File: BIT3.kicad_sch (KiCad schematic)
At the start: 46 parts, among them J1 Conn_02x04_Odd_Even, J2 Conn_01x02_Pin, Q1 2SC1815, SW1 SW_SPDT, SW2 SW_Push, SW3 SW_Push, U2 SG-107F, U3 SG-107F, U4 SG-107F, U5 SG-107F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

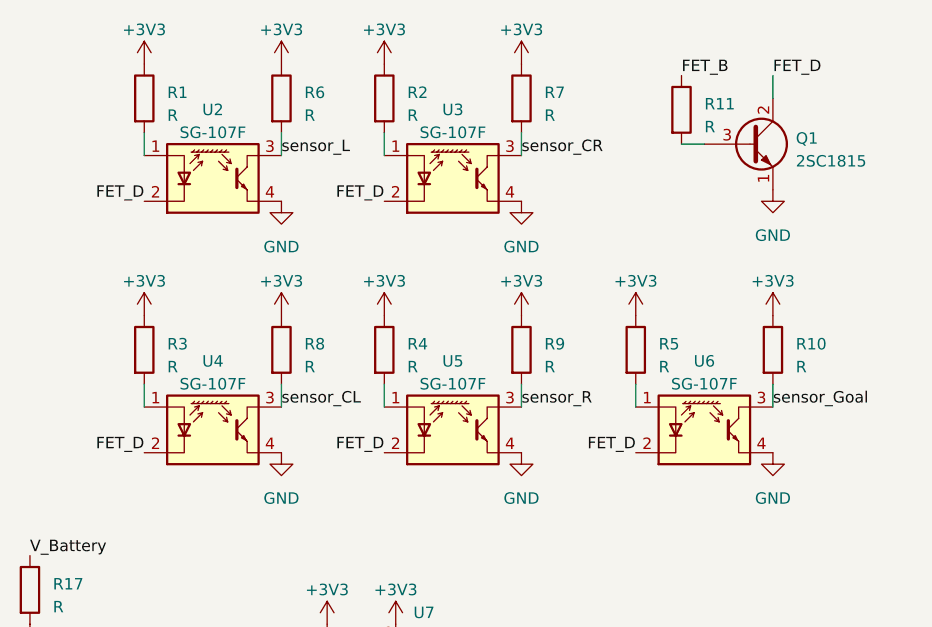
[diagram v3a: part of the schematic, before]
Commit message: フォトセンサを変更
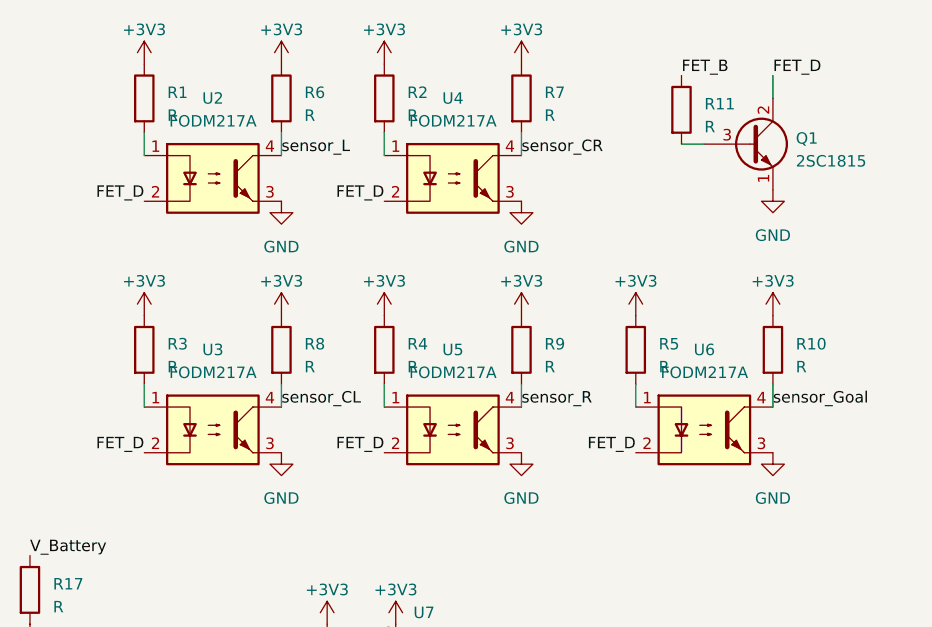
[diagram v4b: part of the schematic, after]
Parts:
- removed U2, U3, U4, U5, U6: SG-107F, OptoDevice:Kodenshi_SG105F, symbol Sensor_Proximity:SG-107F
- added U2, U3, U4, U5, U6: FODM217A, AE-Parts:LBR-127HLD, symbol Isolator:FODM217A
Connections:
- net FET_D: now also U2.2, U3.2, U4.2, U5.2, U6.2
- net GND: now also U2.3, U3.3, U4.3, U5.3, U6.3
- net sensor_CL: now also U3.4
- net sensor_CR: now also U4.4
- net sensor_Goal: now also U6.4
- net sensor_L: now also U2.4
- net sensor_R: now also U5.4
- net at R1.2: now also U2.1
- net at R4.2: now also U5.1
- net at R5.2: now also U6.1
- net at R3.2: now also U3.1
- net at R2.2: now also U4.1

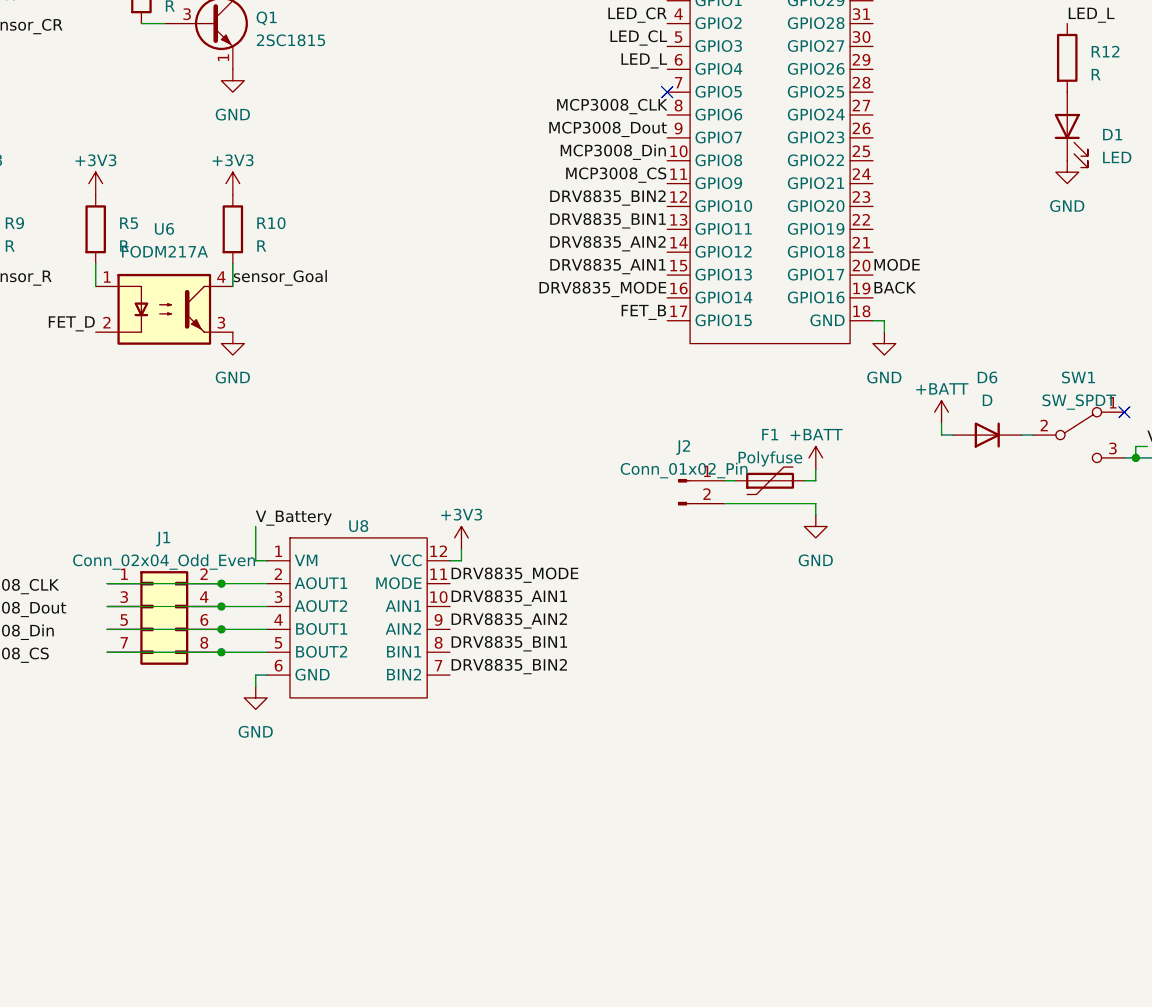
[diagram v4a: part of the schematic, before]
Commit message: XBee を接続できるように変更
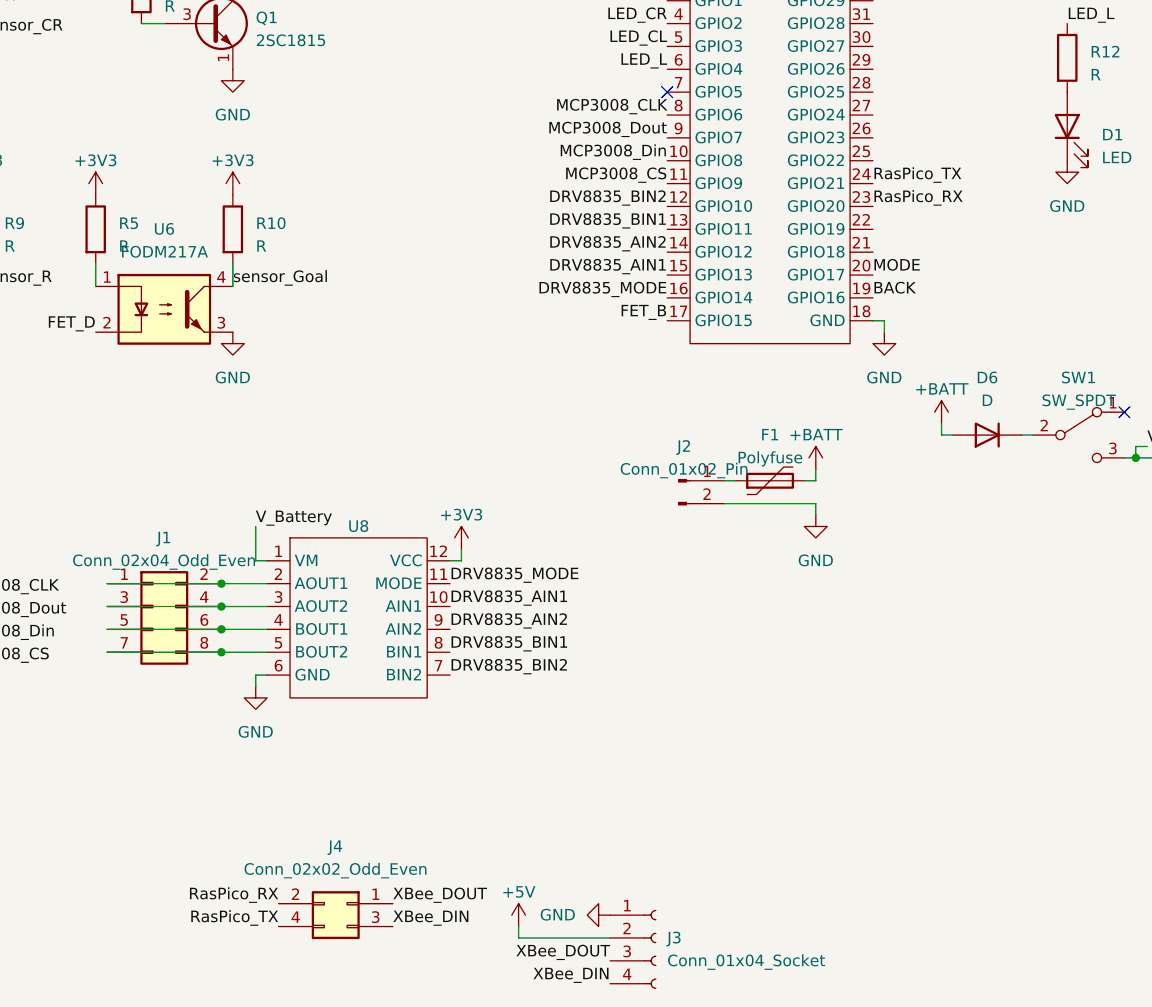
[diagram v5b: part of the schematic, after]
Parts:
- added J3: Conn_01x04_Socket, Connector_PinSocket_2.54mm:PinSocket_1x04_P2.54mm_Vertical, symbol Connector:Conn_01x04_Socket
- added J4: Conn_02x02_Odd_Even, Connector_PinSocket_2.54mm:PinSocket_2x02_P2.54mm_Vertical, symbol Connector_Generic:Conn_02x02_Odd_Even
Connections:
- net +5V: now also J3.2 (Pin_2)
- net GND: now also J3.1 (Pin_1)
- net RasPico_RX: now reaches U1.23 (GPIO20)
- net RasPico_RX: now also J4.2 (Pin_2)
- net RasPico_TX: now reaches U1.24 (GPIO21)
- net RasPico_TX: now also J4.4 (Pin_4)
- new net XBee_DIN: J3.4 (Pin_4), J4.3 (Pin_3)
- new net XBee_DOUT: J3.3 (Pin_3), J4.1 (Pin_1)
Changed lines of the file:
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@@
+    (stroke (width 0) (type default))
+  )
+  (wire (pts (xy 130.81 177.8) (xy 140.97 177.8))
     (stroke (width 0) (type default))
   )
@@
     (stroke (width 0) (type default))
   )
+  (wire (pts (xy 130.81 177.8) (xy 130.81 176.53))
+    (stroke (width 0) (type default))
+  )
   (wire (pts (xy 97.79 146.05) (xy 102.87 146.05))
     (stroke (width 0) (type default))
@@
     (effects (font (size 1.27 1.27)) (justify left bottom))
   )
+  (label "XBee_DIN" (at 140.97 182.88 180) (fields_autoplaced)
+    (effects (font (size 1.27 1.27)) (justify right bottom))
+  )
   (label "MCP3008_Din" (at 67.31 144.78 0) (fields_autoplaced)
     (effects (font (size 1.27 1.27)) (justify left bottom))
@@
     (effects (font (size 1.27 1.27)) (justify left bottom))
   )
+  (label "RasPico_TX" (at 170.18 93.98 0) (fields_autoplaced)
+    (effects (font (size 1.27 1.27)) (justify left bottom))
+  )
   (label "DRV8835_BIN2" (at 123.19 148.59 0) (fields_autoplaced)
     (effects (font (size 1.27 1.27)) (justify left bottom))
@@
     (effects (font (size 1.27 1.27)) (justify left bottom))
   )
+  (label "XBee_DOUT" (at 116.84 173.99 0) (fields_autoplaced)
+    (effects (font (size 1.27 1.27)) (justify left bottom))
+  )
   (label "FET_D" (at 55.88 110.49 180) (fields_autoplaced)
     (effects (font (size 1.27 1.27)) (justify right bottom))
@@
     (effects (font (size 1.27 1.27)) (justify right bottom))
   )
+  (label "RasPico_RX" (at 170.18 96.52 0) (fields_autoplaced)
+    (effects (font (size 1.27 1.27)) (justify left bottom))
+  )
   (label "sensor_R" (at 36.83 137.16 180) (fields_autoplaced)
     (effects (font (size 1.27 1.27)) (justify right bottom))
@@
     (effects (font (size 1.27 1.27)) (justify right bottom))
   )
+  (label "RasPico_RX" (at 104.14 173.99 180) (fields_autoplaced)
+    (effects (font (size 1.27 1.27)) (justify right bottom))
+  )
   (label "MCP3008_CLK" (at 147.32 86.36 180) (fields_autoplaced)
     (effects (font (size 1.27 1.27)) (justify right bottom))
@@
     (effects (font (size 1.27 1.27)) (justify right bottom))
   )
+  (label "XBee_DIN" (at 116.84 176.53 0) (fields_autoplaced)
+    (effects (font (size 1.27 1.27)) (justify left bottom))
+  )
   (label "FET_D" (at 55.88 82.55 180) (fields_autoplaced)
     (effects (font (size 1.27 1.27)) (justify right bottom))
@@
     (effects (font (size 1.27 1.27)) (justify right bottom))
   )
+  (label "XBee_DOUT" (at 140.97 180.34 180) (fields_autoplaced)
+    (effects (font (size 1.27 1.27)) (justify right bottom))
+  )
   (label "LED_Goal" (at 237.49 76.2 0) (fields_autoplaced)
     (effects (font (size 1.27 1.27)) (justify left bottom))
+  )
+  (label "RasPico_TX" (at 104.14 176.53 180) (fields_autoplaced)
+    (effects (font (size 1.27 1.27)) (justify right bottom))
   )
   (label "LED_CL" (at 203.2 76.2 0) (fields_autoplaced)
@@
     )
   )
+  (symbol (lib_id "Connector_Generic:Conn_02x02_Odd_Even") (at 111.76 173.99 0) (mirror y) (unit 1)
+    (in_bom yes) (on_board yes) (dnp no)
+    (property "Reference" "J4" (at 110.49 167.64 0)
+      (effects (font (size 1.27 1.27)))
+    )
+    (property "Value" "Conn_02x02_Odd_Even" (at 110.49 170.18 0)
+      (effects (font (size 1.27 1.27)))
+    )
+    (property "Footprint" "Connector_PinSocket_2.54mm:PinSocket_2x02_P2.54mm_Vertical" (at 111.76 173.99 0)
+      (effects (font (size 1.27 1.27)) hide)
+    )
+    (property "Datasheet" "~" (at 111.76 173.99 0)
+      (effects (font (size 1.27 1.27)) hide)
+    )
+    (pin "1")
+    (pin "2")
+    (pin "3")
+    (pin "4")
+    (instances
+      (project "BIT3"
+        (path "/e911d5a5-765c-4e39-aa6a-9a13739432fd"
+          (reference "J4") (unit 1)
+        )
+      )
+    )
+  )
   (symbol (lib_id "power:GND") (at 101.6 149.86 0) (unit 1)
     (in_bom yes) (on_board yes) (dnp no) (fields_autoplaced)
@@
     )
   )
+  (symbol (lib_id "Connector:Conn_01x04_Socket") (at 146.05 177.8 0) (unit 1)
+    (in_bom yes) (on_board yes) (dnp no) (fields_autoplaced)
+    (property "Reference" "J3" (at 147.32 177.8 0)
+      (effects (font (size 1.27 1.27)) (justify left))
+    )
+    (property "Value" "Conn_01x04_Socket" (at 147.32 180.34 0)
+      (effects (font (size 1.27 1.27)) (justify left))
+    )
+    (property "Footprint" "Connector_PinSocket_2.54mm:PinSocket_1x04_P2.54mm_Vertical" (at 146.05 177.8 0)
+      (effects (font (size 1.27 1.27)) hide)
+    )
+    (property "Datasheet" "~" (at 146.05 177.8 0)
+      (effects (font (size 1.27 1.27)) hide)
+    )
+    (pin "1")
+    (pin "2")
+    (pin "3")
+    (pin "4")
+    (instances
+      (project "BIT3"
+        (path "/e911d5a5-765c-4e39-aa6a-9a13739432fd"
+          (reference "J3") (unit 1)
+        )
+      )
+    )
+  )
   (symbol (lib_id "Device:R") (at 71.12 99.06 0) (unit 1)
     (in_bom yes) (on_board yes) (dnp no) (fields_autoplaced)
@@
         (path "/e911d5a5-765c-4e39-aa6a-9a13739432fd"
           (reference "#PWR047") (unit 1)
+        )
+      )
+    )
+  )
+  (symbol (lib_id "power:+5V") (at 130.81 176.53 0) (unit 1)
+    (in_bom yes) (on_board yes) (dnp no) (fields_autoplaced)
+    (property "Reference" "#PWR05" (at 130.81 180.34 0)
+      (effects (font (size 1.27 1.27)) hide)
+    )
+    (property "Value" "+5V" (at 130.81 172.72 0)
+      (effects (font (size 1.27 1.27)))
+    )
+    (property "Footprint" "" (at 130.81 176.53 0)
+      (effects (font (size 1.27 1.27)) hide)
+    )
+    (property "Datasheet" "" (at 130.81 176.53 0)
+      (effects (font (size 1.27 1.27)) hide)
+    )
+    (pin "1")
+    (instances
+      (project "BIT3"
+        (path "/e911d5a5-765c-4e39-aa6a-9a13739432fd"
+          (reference "#PWR05") (unit 1)
         )
       )
@@
         )
       )
+    )
+  )
+  (symbol (lib_id "power:GND") (at 140.97 175.26 270) (unit 1)
+    (in_bom yes) (on_board yes) (dnp no) (fields_autoplaced)
+    (property "Reference" "#PWR027" (at 134.62 175.26 0)
+      (effects (font (size 1.27 1.27)) hide)
+    )
+    (property "Value" "GND" (at 137.16 175.26 90)
+      (effects (font (size 1.27 1.27)) (justify right))
+    )
+    (property "Footprint" "" (at 140.97 175.26 0)
+      (effects (font (size 1.27 1.27)) hide)
+    )
+    (property "Datasheet" "" (at 140.97 175.26 0)
+      (effects (font (size 1.27 1.27)) hide)
+    )
+    (pin "1")
+    (instances
+      (project "BIT3"
+        (path "/e911d5a5-765c-4e39-aa6a-9a13739432fd"
+          (reference "#PWR027") (unit 1)
+        )
+      )

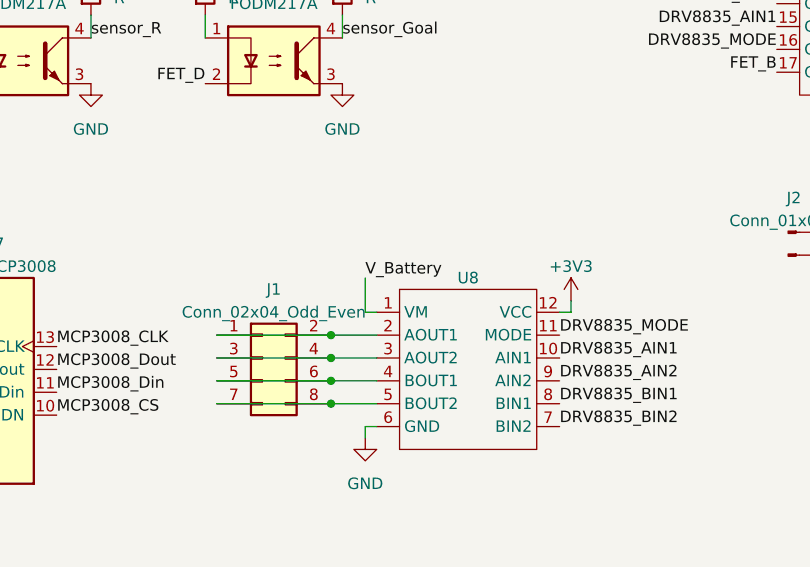
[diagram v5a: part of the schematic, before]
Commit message: モータの電源を BATT から 5V に変更
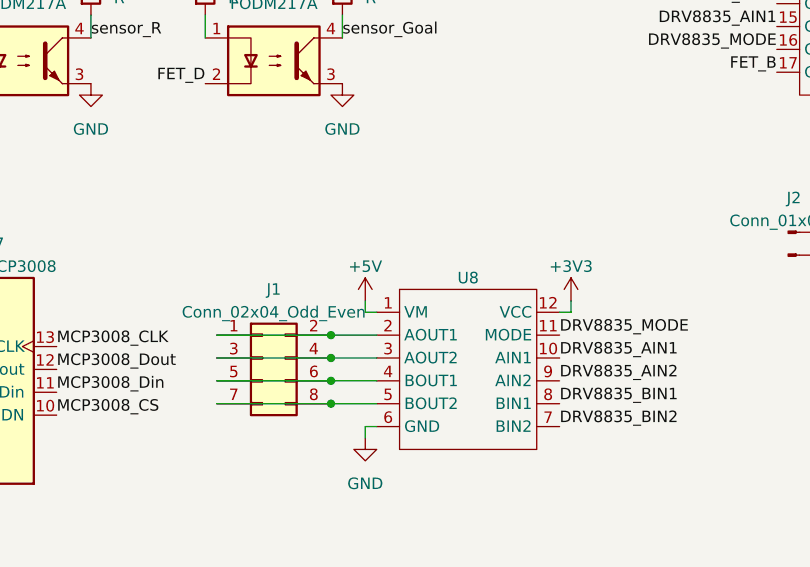
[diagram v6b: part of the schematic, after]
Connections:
- net +5V: now also U8.1 (VM)
- net V_Battery: no longer U8.1 (VM)
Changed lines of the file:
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@@
     (stroke (width 0) (type default))
   )
-  (wire (pts (xy 101.6 135.89) (xy 101.6 132.08))
+  (wire (pts (xy 101.6 135.89) (xy 101.6 134.62))
     (stroke (width 0) (type default))
   )
@@
   (label "LED_R" (at 147.32 73.66 180) (fields_autoplaced)
     (effects (font (size 1.27 1.27)) (justify right bottom))
-  )
-  (label "V_Battery" (at 101.6 132.08 0) (fields_autoplaced)
-    (effects (font (size 1.27 1.27)) (justify left bottom))
   )
   (label "sensor_Goal" (at 99.06 105.41 0) (fields_autoplaced)
@@
         )
       )
+    )
+  )
+  (symbol (lib_id "power:+5V") (at 101.6 134.62 0) (unit 1)
+    (in_bom yes) (on_board yes) (dnp no) (fields_autoplaced)
+    (property "Reference" "#PWR028" (at 101.6 138.43 0)
+      (effects (font (size 1.27 1.27)) hide)
+    )
+    (property "Value" "+5V" (at 101.6 130.81 0)
+      (effects (font (size 1.27 1.27)))
+    )
+    (property "Footprint" "" (at 101.6 134.62 0)
+      (effects (font (size 1.27 1.27)) hide)
+    )
+    (property "Datasheet" "" (at 101.6 134.62 0)
+      (effects (font (size 1.27 1.27)) hide)
+    )
+    (pin "1")
+    (instances
+      (project "BIT3"
+        (path "/e911d5a5-765c-4e39-aa6a-9a13739432fd"
+          (reference "#PWR028") (unit 1)
+        )
+      )

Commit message: モータ電源を BATT に戻した
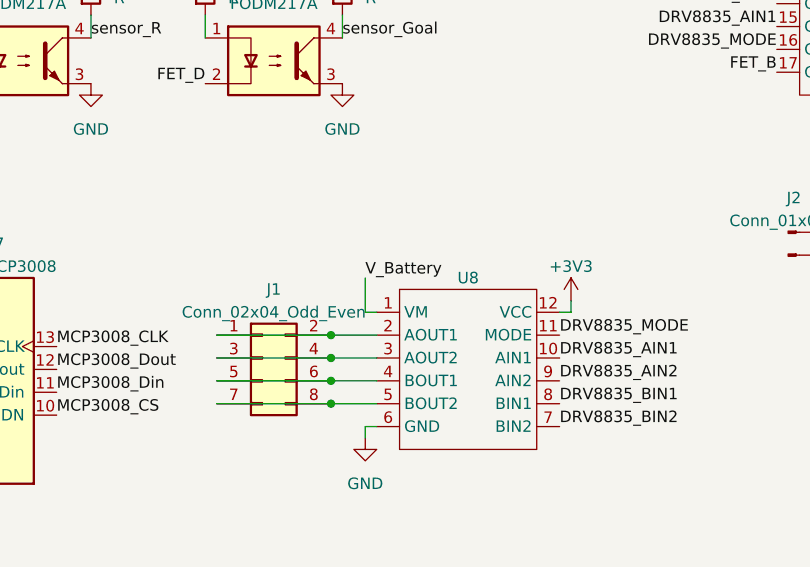
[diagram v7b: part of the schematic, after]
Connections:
- net +5V: no longer U8.1 (VM)
- net V_Battery: now also U8.1 (VM)
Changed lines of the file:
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@@
     (stroke (width 0) (type default))
   )
-  (wire (pts (xy 101.6 135.89) (xy 101.6 134.62))
+  (wire (pts (xy 101.6 132.08) (xy 101.6 135.89))
     (stroke (width 0) (type default))
   )
@@
   (label "RasPico_TX" (at 104.14 176.53 180) (fields_autoplaced)
     (effects (font (size 1.27 1.27)) (justify right bottom))
+  )
+  (label "V_Battery" (at 101.6 132.08 0) (fields_autoplaced)
+    (effects (font (size 1.27 1.27)) (justify left bottom))
   )
   (label "LED_CL" (at 203.2 76.2 0) (fields_autoplaced)
@@
         )
       )
-    )
-  )
-  (symbol (lib_id "power:+5V") (at 101.6 134.62 0) (unit 1)
-    (in_bom yes) (on_board yes) (dnp no) (fields_autoplaced)
-    (property "Reference" "#PWR028" (at 101.6 138.43 0)
-      (effects (font (size 1.27 1.27)) hide)
-    )
-    (property "Value" "+5V" (at 101.6 130.81 0)
-      (effects (font (size 1.27 1.27)))
-    )
-    (property "Footprint" "" (at 101.6 134.62 0)
-      (effects (font (size 1.27 1.27)) hide)
-    )
-    (property "Datasheet" "" (at 101.6 134.62 0)
-      (effects (font (size 1.27 1.27)) hide)
-    )
-    (pin "1")
-    (instances
-      (project "BIT3"
-        (path "/e911d5a5-765c-4e39-aa6a-9a13739432fd"
-          (reference "#PWR028") (unit 1)
-        )
-      )
